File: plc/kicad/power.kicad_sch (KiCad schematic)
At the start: 67 parts, among them Q5 BSS138LT1G, Q6 CSD19537Q3, SW3 TSD003B08026A03, U11 LMR16006XDDCR, U12 TPS54560DDAR, U13 TPS26630RGER, U17 TLV76733DRVR

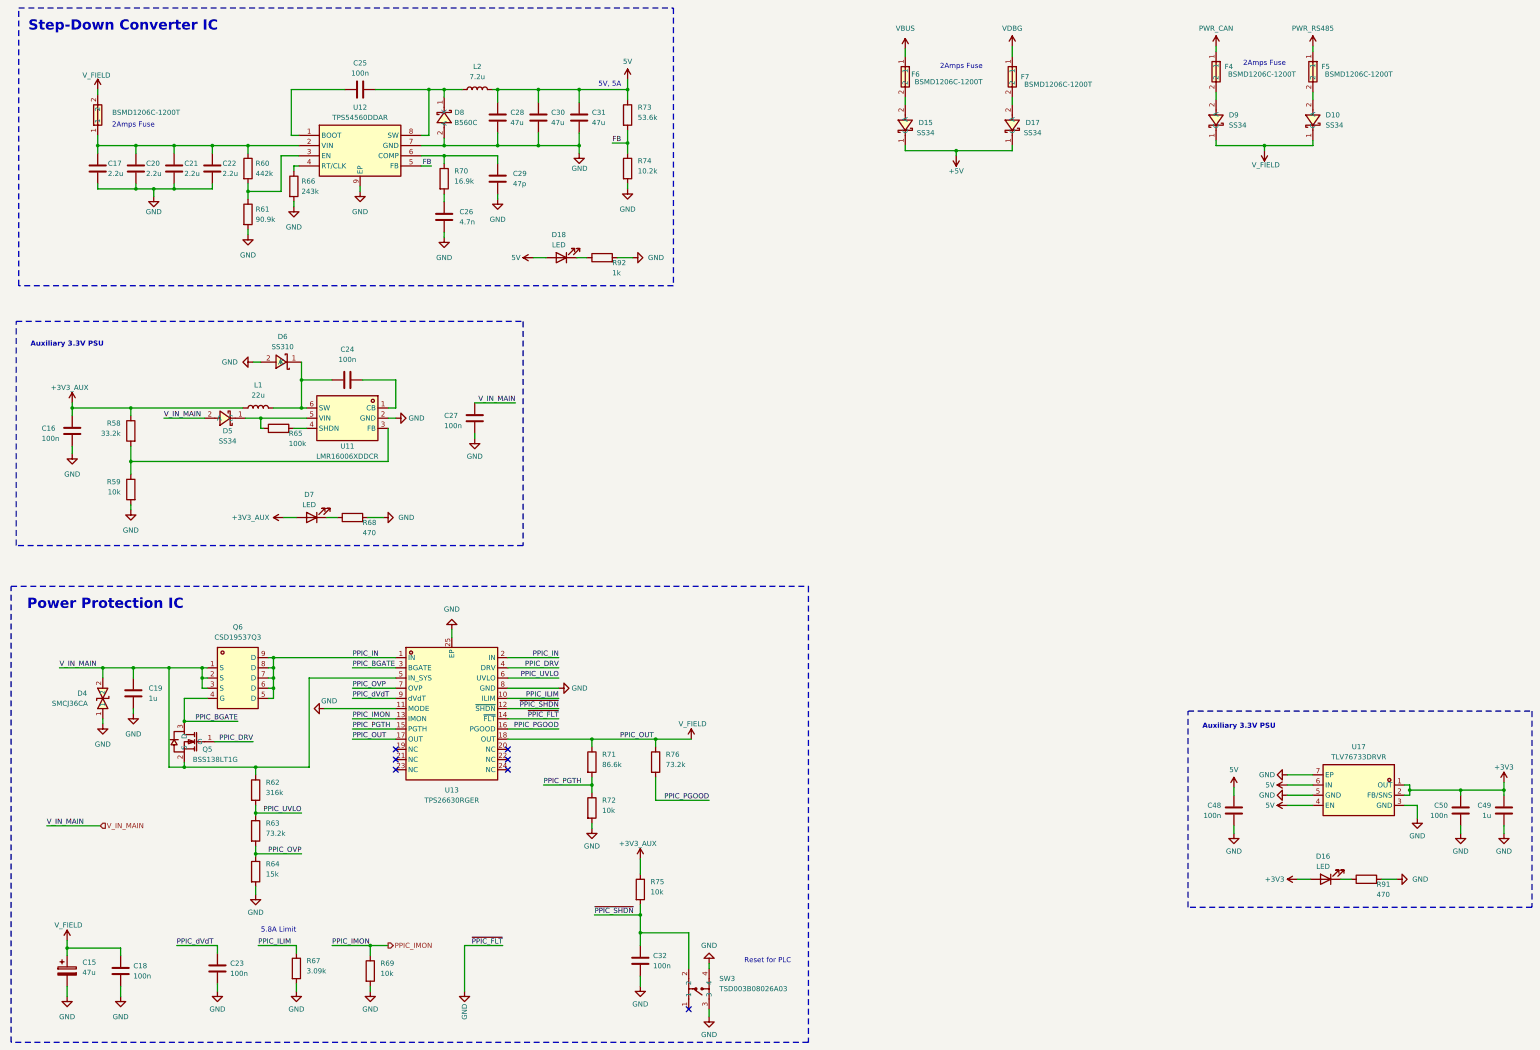
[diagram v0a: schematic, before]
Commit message: Added more testpads
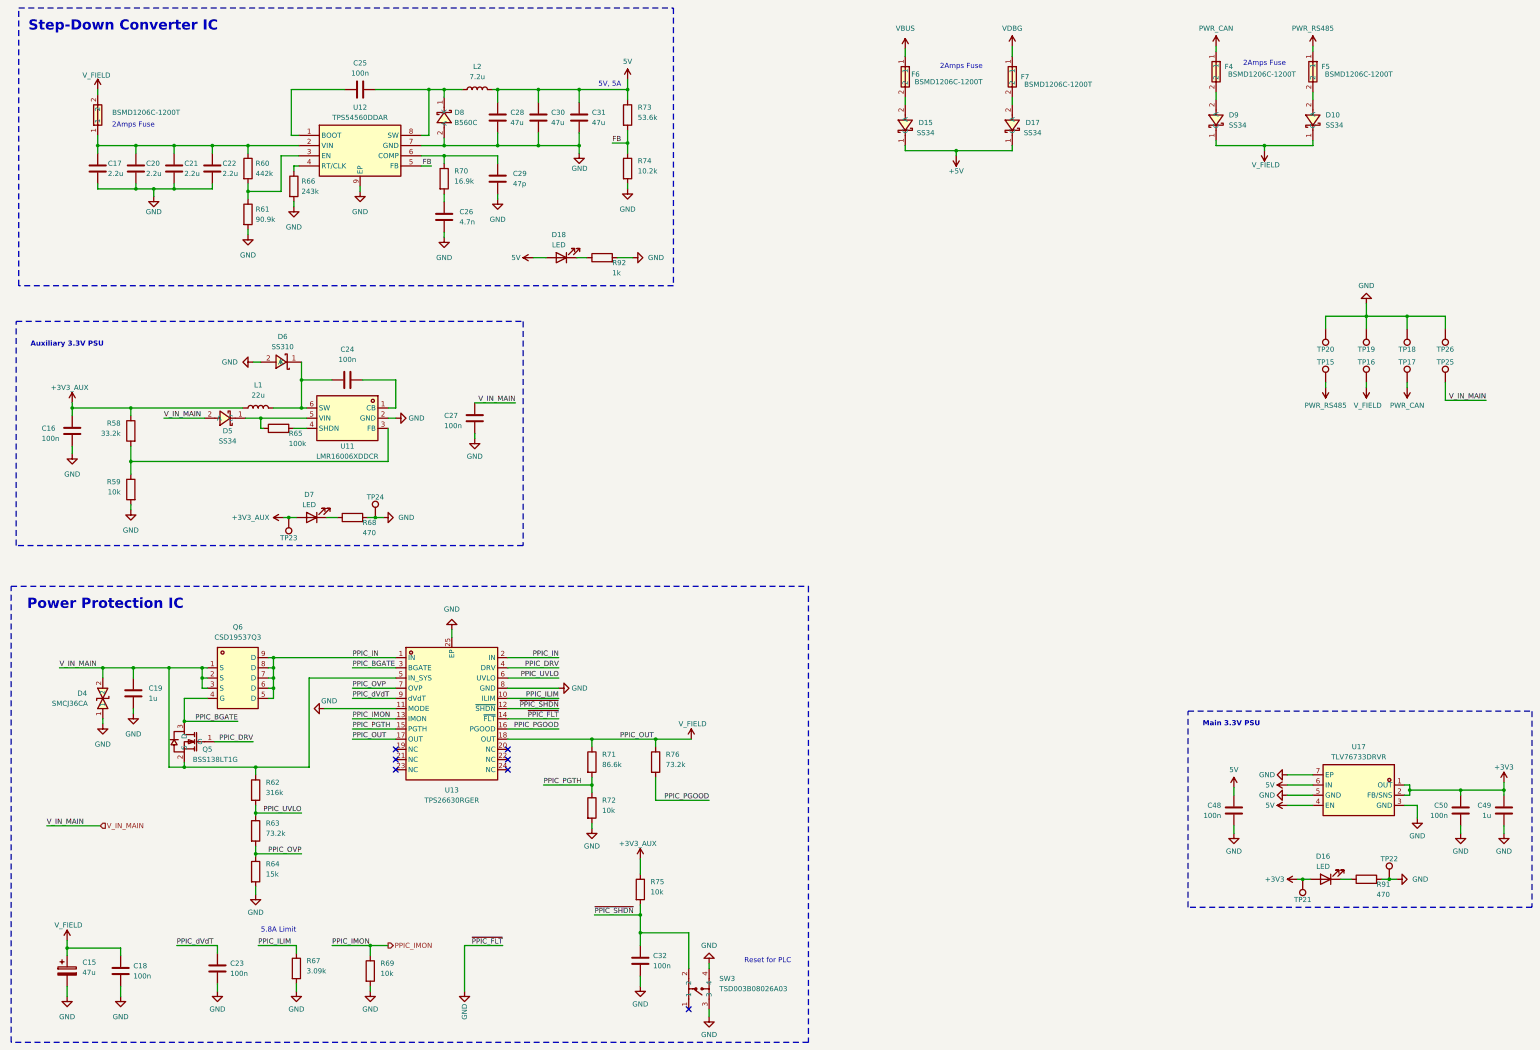
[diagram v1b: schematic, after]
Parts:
- added TP15, TP16, TP17, TP18, TP19, TP20, TP25, TP26: TestPoint, TestPoint:TestPoint_Pad_D4.0mm, symbol Connector:TestPoint
- added TP21, TP22, TP23, TP24: TestPoint, TestPoint:TestPoint_Pad_D3.0mm, symbol Connector:TestPoint
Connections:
- net +3V3: now also TP21.1
- net +3V3_AUX: now also TP23.1
- net GND: now also TP18.1, TP19.1, TP20.1, TP22.1, TP24.1, TP26.1
- net PWR_CAN: now also TP17.1
- net PWR_RS485: now also TP15.1
- net V_FIELD: now also TP16.1
- net V_IN_MAIN: now also TP25.1
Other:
- note added: "Main 3.3V PSU"

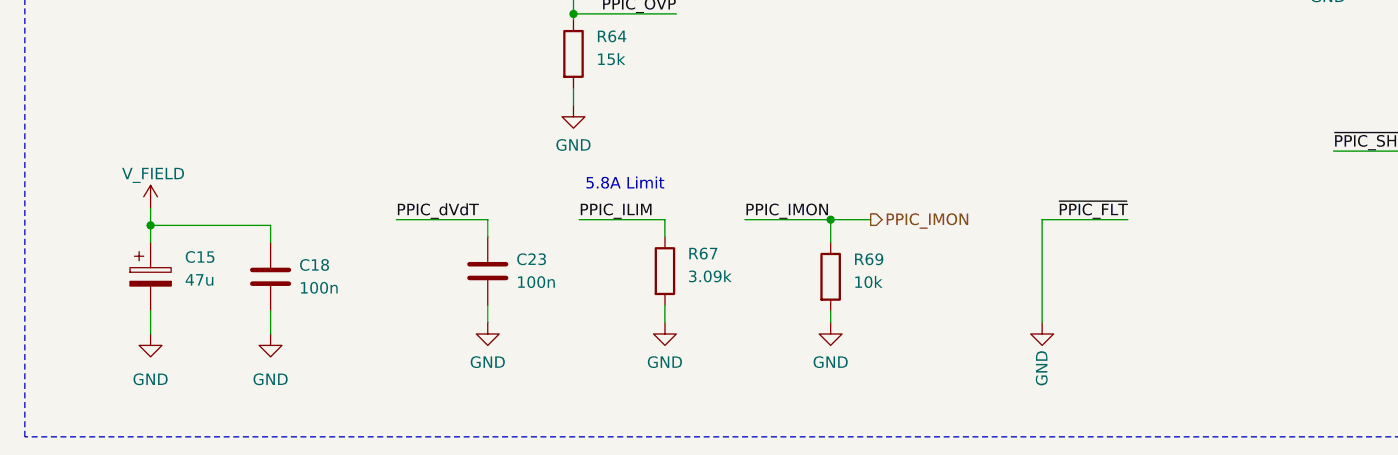
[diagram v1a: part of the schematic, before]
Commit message: Added RTC IC
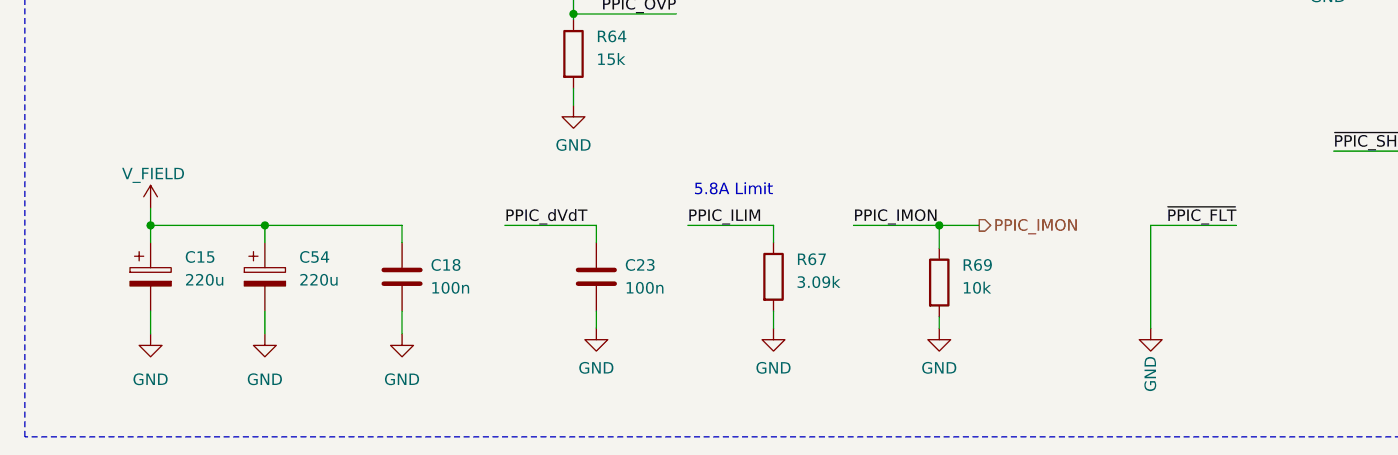
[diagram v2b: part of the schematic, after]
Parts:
- added C54: 220u, Capacitor_SMD:C_0603_1608Metric, symbol Device:C_Polarized
- C15: value 47u -> 220u; LCSC Part (none) -> C125977
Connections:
- net GND: now also C54.2
- net V_FIELD: now also C54.1
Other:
- moved on the sheet: C18, C23, R67, R69

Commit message: PCB placement
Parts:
- added TP21, TP22: TestPoint, TestPoint:TestPoint_Pad_D3.0mm, symbol Connector:TestPoint
- renumbered C15 to C18, C16 to C19, C17 to C20, C54 to C21, C19 to C22, C20 to C23, C21 to C24, C18 to C25, C22 to C26, C23 to C27, C24 to C28, C25 to C29, C26 to C30, C27 to C31, C28 to C32, C29 to C33, C30 to C34, C31 to C35, C32 to C36, C48 to C37, C50 to C38, C49 to C39, D15 to D10, D17 to D11, D9 to D12, D10 to D13, D16 to D14, D18 to D9, F6 to F3, F7 to F4, F4 to F5, F5 to F6, R58 to R59, R59 to R60, R60 to R61, R61 to R62, R62 to R63, R63 to R64, R64 to R65, R65 to R66, R66 to R67, R67 to R68, R68 to R69, R69 to R70, R70 to R71, R71 to R72, R72 to R73, R92 to R74, R73 to R75, R74 to R76, R75 to R77, R76 to R78, R91 to R79, TP23 to TP19, TP24 to TP20, TP21 to TP23, TP20 to TP24, TP15 to TP25, TP19 to TP26, TP16 to TP27, TP22 to TP28, TP18 to TP29, TP17 to TP30, TP26 to TP31, TP25 to TP32, U11 to U14, U12 to U15, U13 to U16
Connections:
- net 5V: now also TP21.1
- net GND: now also TP22.1
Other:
- title: (none) -> LibrePLC32
